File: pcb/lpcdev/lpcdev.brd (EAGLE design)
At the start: 100 x 80 mm, 106 parts, among them IC1 LPC1517BJD48, IC2 DRV8313, IC3 FT231X, IC4 LP2985-3V3, IC5 DRV8313, IC6 DRV8313, Q1 16MHz

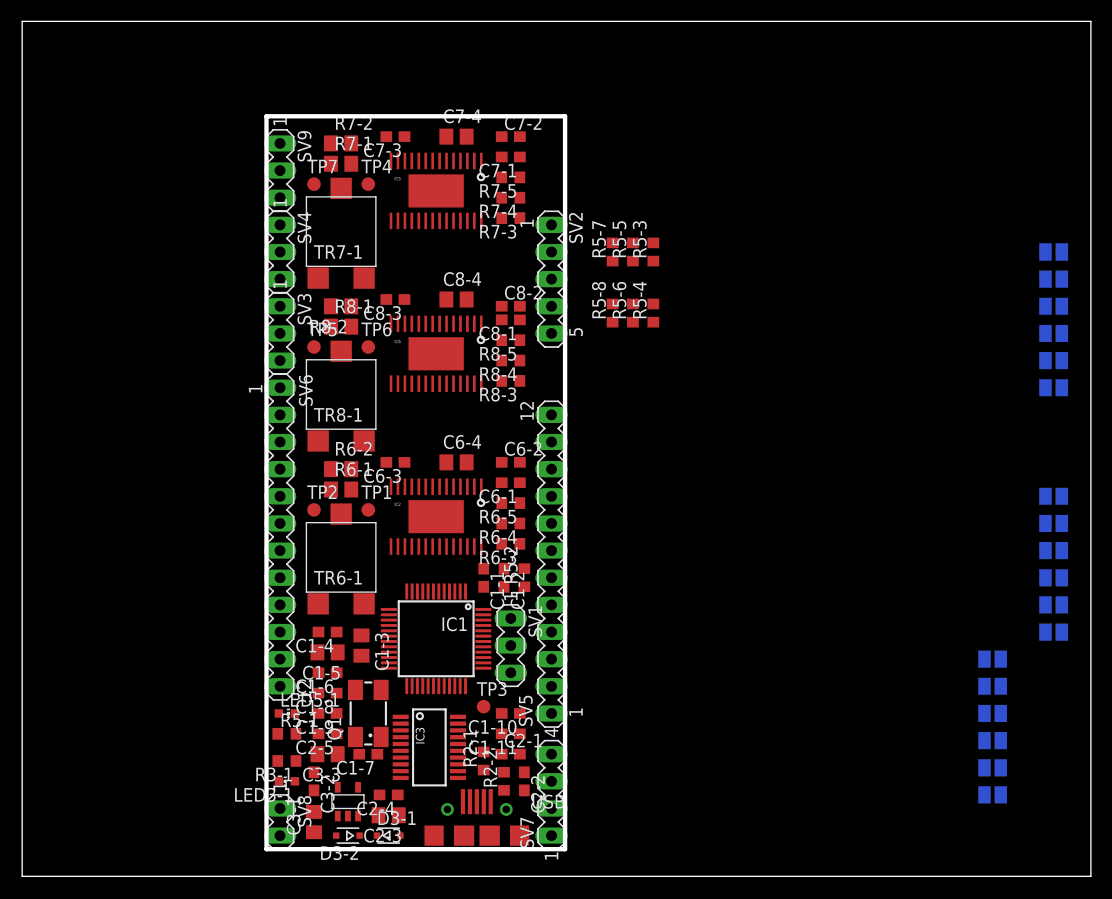
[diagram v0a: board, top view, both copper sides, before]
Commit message: rough routing (no gnd)
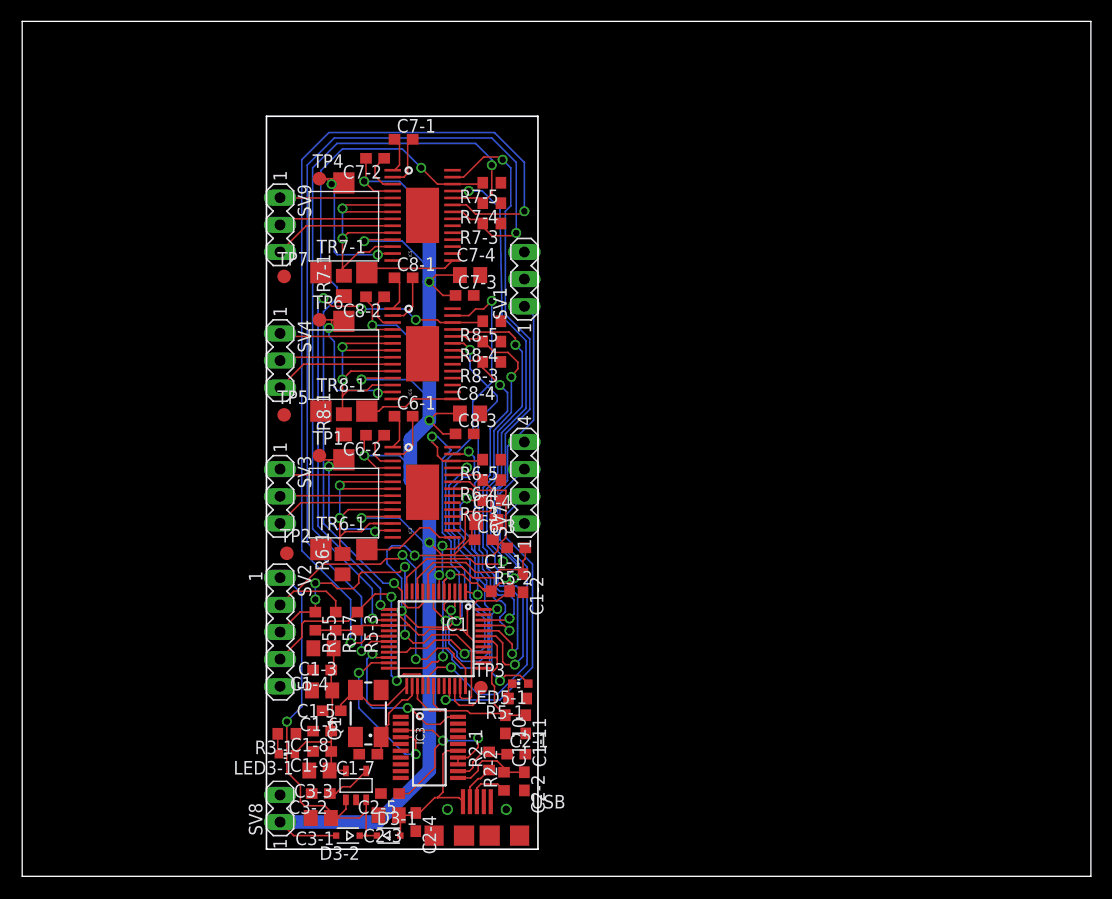
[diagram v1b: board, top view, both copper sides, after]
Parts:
- removed R5-4, R5-6, R5-8: DNM, rcl:R0603
- removed R6-2, R7-2, R8-2: TBD, rcl:R0805
- removed SJ6-1, SJ6-2, SJ6-3, SJ6-4, SJ6-5, SJ6-6, SJ7-1, SJ7-2, SJ7-3, SJ7-4, SJ7-5, SJ7-6, SJ8-1, SJ8-2, SJ8-3, SJ8-4, SJ8-5, SJ8-6: (no value), jumper:SJ
- removed SV5: P1, con-lstb:MA12-1
- removed SV6: P2, con-lstb:MA12-1
- moved R5-5 45.6 mm to (27.4, 23.9), turned to 270 degrees
- moved R5-3 44.3 mm to (31.4, 23.9), turned to 270 degrees
- moved R5-7 43.2 mm to (29.3, 23.9), turned to 270 degrees
- moved SV2 41.7 mm to (24.1, 22.9)
- moved SV1 34.3 mm to (47.0, 55.9), turned to 90 degrees
- moved SV7 29.3 mm to (47.0, 36.8)
- moved LED5-1 22.0 mm to (46.6, 18.0), turned to 90 degrees
- moved R5-1 21.8 mm to (46.4, 16.6), turned to 180 degrees
- moved C7-3 16.2 mm to (41.4, 54.4), turned to 0 degrees
- moved SV3 15.2 mm to (24.1, 35.6)
- moved C8-3 14.1 mm to (41.4, 41.4), turned to 0 degrees
- moved C7-4 13.0 mm to (41.9, 56.3)
- moved C6-2 13.0 mm to (33.0, 41.3), turned to 180 degrees
- moved C7-2 12.9 mm to (33.0, 67.2), turned to 180 degrees
- moved C8-2 12.7 mm to (33.0, 54.2), turned to 180 degrees
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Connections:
- removed net PIO0_0: IC1.1, SJ6-1.2, SV5.2
- removed net PIO0_1: IC1.2, SJ6-2.2, SV5.3
- removed net PIO0_10: IC1.15, SJ7-4.2, SV5.11
- removed net PIO0_11: IC1.18, SJ7-5.2, SV6.1
- removed net PIO0_12: IC1.19, SJ7-6.2, SV6.2
- removed net PIO0_13: IC1.21, SJ8-1.2, SV6.3
- removed net PIO0_18: IC1.13, SJ8-2.2, SV6.4
- removed net PIO0_2: IC1.3, SJ6-3.2, SV5.4
- removed net PIO0_24: IC1.43, SJ8-3.2, SV6.7
- removed net PIO0_25: IC1.44, SJ8-4.2, SV6.8
- removed net PIO0_26: IC1.45, SJ8-5.2, SV6.9
- removed net PIO0_27: IC1.46, SJ8-6.2, SV6.10
- removed net PIO0_3: IC1.4, SJ6-4.2, SV5.5
- removed net PIO0_5: IC1.6, SJ6-5.2, SV5.6
- removed net PIO0_6: IC1.7, SJ6-6.2, SV5.7
- removed net PIO0_7: IC1.8, SJ7-1.2, SV5.8
- removed net PIO0_8: IC1.9, SJ7-2.2, SV5.9
- removed net PIO0_9: IC1.12, SJ7-3.2, SV5.10
- net +3V3: no longer SV5.1
- net DRV1_3V3: now also TR6-1.2; no longer TR6-1.1
- net DRV1_COMPP: no longer R6-2.2
- net DRV1_EN1: now also IC1.2; no longer SJ6-2.1
- net DRV1_EN2: now also IC1.4; no longer SJ6-4.1
- net DRV1_EN3: now also IC1.7; no longer SJ6-6.1
- net DRV1_IN1: now also IC1.1; no longer SJ6-1.1
- net DRV1_IN2: now also IC1.3; no longer SJ6-3.1
- net DRV1_IN3: now also IC1.6; no longer SJ6-5.1
- net DRV2_3V1: now also TR7-1.2; no longer TR7-1.1
- net DRV2_COMPP1: no longer R7-2.2
- net DRV2_EN1: now also IC1.9; no longer SJ7-2.1
- net DRV2_EN2: now also IC1.15; no longer SJ7-4.1
- net DRV2_EN3: now also IC1.19; no longer SJ7-6.1
- net DRV2_IN1: now also IC1.8; no longer SJ7-1.1
- net DRV2_IN2: now also IC1.12; no longer SJ7-3.1
- net DRV2_IN3: now also IC1.18; no longer SJ7-5.1
- net DRV3_3V2: now also TR8-1.2; no longer TR8-1.1
- net DRV3_COMPP2: no longer R8-2.2
- net DRV3_EN1: now also IC1.13; no longer SJ8-2.1
- net DRV3_EN2: now also IC1.44; no longer SJ8-4.1
- net DRV3_EN3: now also IC1.46; no longer SJ8-6.1
- net DRV3_IN1: now also IC1.21; no longer SJ8-1.1
- net DRV3_IN2: now also IC1.43; no longer SJ8-3.1
- net DRV3_IN3: now also IC1.45; no longer SJ8-5.1
- net GND: now also TR6-1.1, TR7-1.1, TR8-1.1; no longer R5-4.1, R5-6.1, R5-8.1, R6-2.1, R7-2.1, R8-2.1, SV5.12, TR6-1.2, TR7-1.2, TR8-1.2
- net PIO0_22: no longer SV6.5
- net PIO0_23: no longer SV6.6
- net PIO0_28: no longer SV6.11
- net PIO0_29: no longer SV6.12
- net QEI_IDX: no longer R5-4.2
- net QEI_PHA: no longer R5-8.2
- net QEI_PHB: no longer R5-6.2
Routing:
- net +12V: track 0.00 -> 159.2 mm, vias 0 -> 9
- net +3V3: track 0.00 -> 87.1 mm
- net DRV2_EN3: track 0.00 -> 85.8 mm, vias 0 -> 2
- net DRV2_IN3: track 0.00 -> 85.7 mm, vias 0 -> 2
- net DRV2_EN2: track 0.00 -> 71.9 mm, vias 0 -> 2
- net DRV2_EN1: track 0.00 -> 66.0 mm, vias 0 -> 2
- net DRV2_IN1: track 0.00 -> 58.4 mm, vias 0 -> 2
- net DRV2_IN2: track 0.00 -> 52.3 mm, vias 0 -> 2
- net ISP_01: track 0.00 -> 51.1 mm, vias 0 -> 3
- net DRV3_IN1: track 0.00 -> 50.3 mm, vias 0 -> 2
- net DRV3_EN1: track 0.00 -> 48.2 mm, vias 0 -> 4
- net DRV3_IN2: track 0.00 -> 46.0 mm, vias 0 -> 2
- net DRV3_EN2: track 0.00 -> 42.1 mm, vias 0 -> 2
- net DRV1_EN2: track 0.00 -> 37.9 mm, vias 0 -> 2
- net REG_VIN: track 0.00 -> 37.9 mm, vias 0 -> 1
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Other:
- outline, holes or cut-outs redrawn

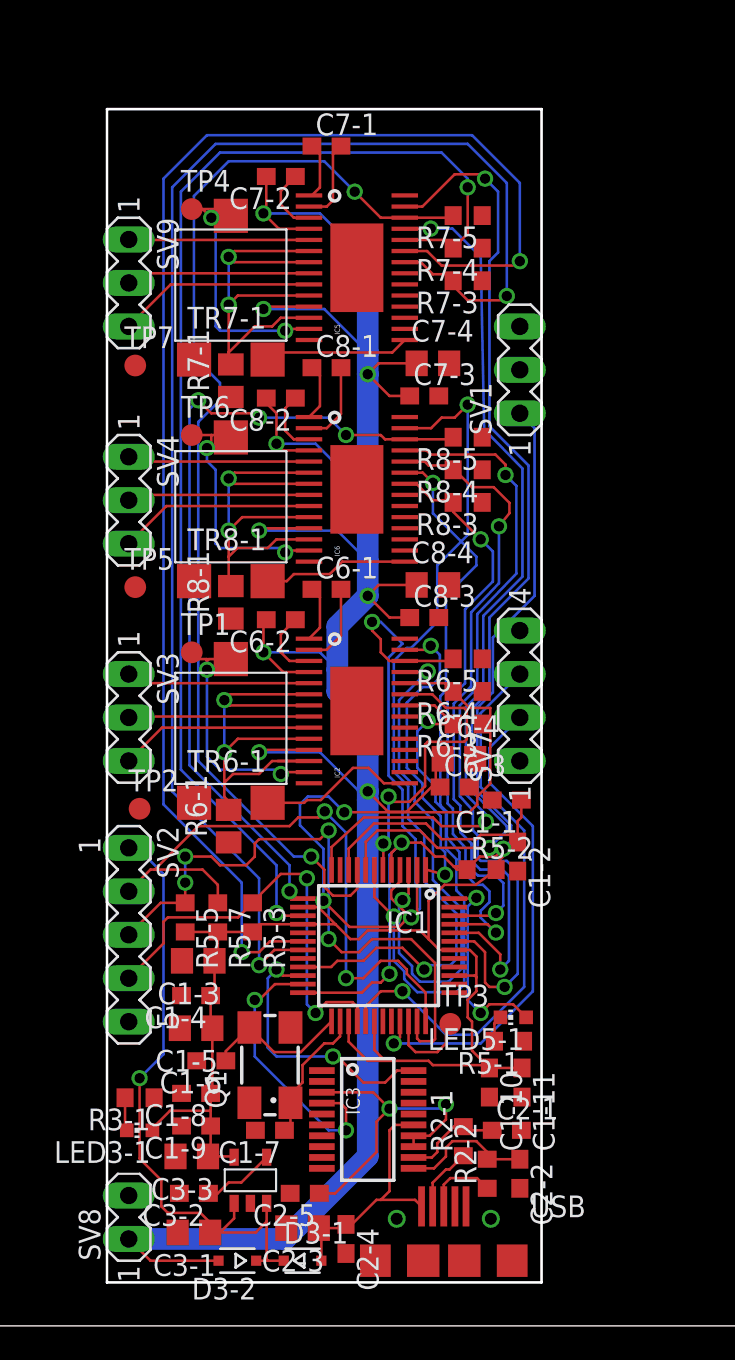
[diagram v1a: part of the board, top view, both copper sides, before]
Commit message: Routing complete, ERC and DRC is OK
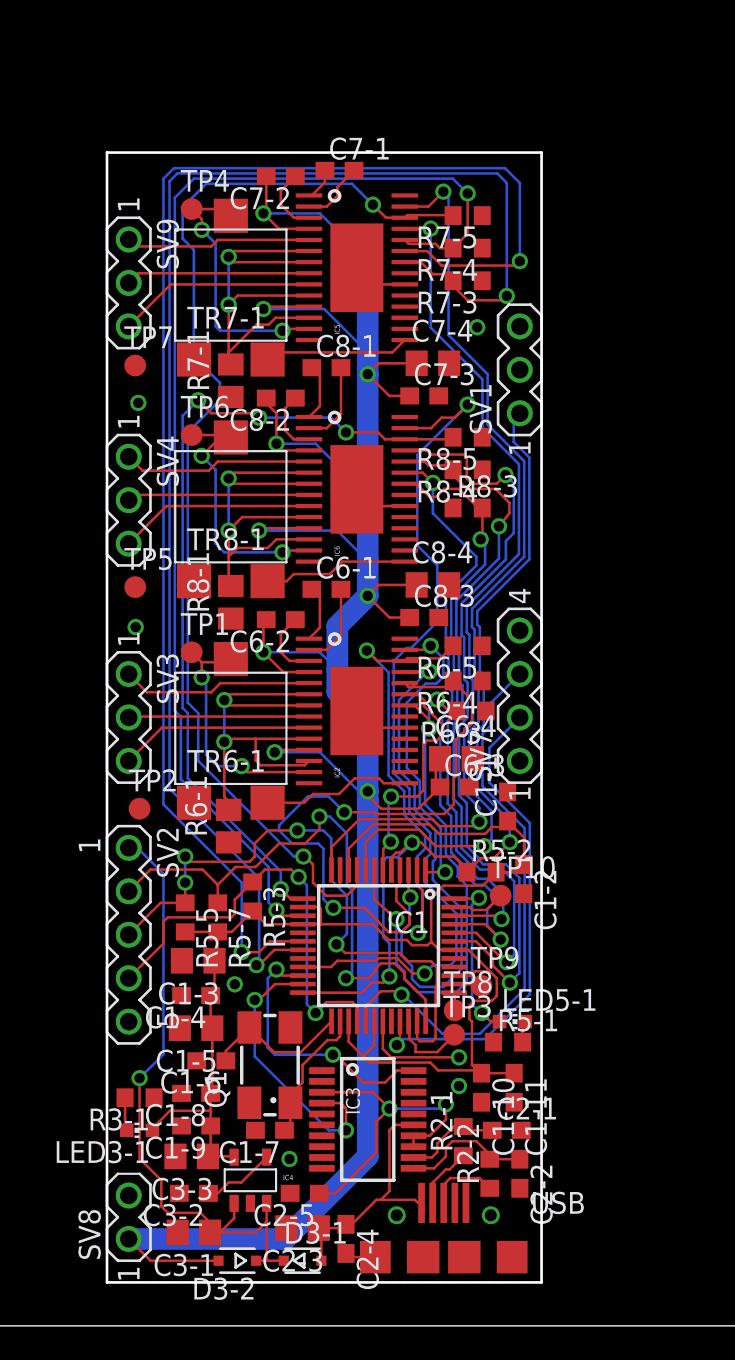
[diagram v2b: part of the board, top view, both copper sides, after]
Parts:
- added TP10, TP8, TP9: TPB1,27, testpad:B1,27
- SV1, SV3, SV4, SV9: device con-lstb:MA03-1 -> lpclib:MA03-1
- SV2: device con-lstb:MA05-1 -> lpclib:MA05-1
- SV7: device con-lstb:MA04-1 -> lpclib:MA04-1
- moved C7-1 1.61 mm to (36.4, 67.5)
- moved C1-2 1.37 mm to (47.2, 26.1)
- moved R5-3 1.22 mm to (31.4, 25.1)
- moved R6-3 0.80 mm to (44.2, 35.9)
- moved R6-5 0.76 mm to (43.9, 39.8)
- moved TP3 0.67 mm to (43.2, 17.0)
- moved R6-4 0.61 mm to (43.9, 37.7)
- moved C1-10 0.55 mm to (44.8, 13.9)
- moved C1-11 0.55 mm to (46.7, 13.9)
- moved C1-1 0.38 mm to (46.3, 30.4), turned to 90 degrees
- moved R8-3 0.33 mm to (43.9, 47.8), turned to 0 degrees
- moved LED5-1 0.26 mm to (46.6, 17.8), turned to 270 degrees
- moved USB 0.20 mm to (42.5, 4.01)
- moved C6-4 0.15 mm to (43.3, 33.1)
- moved R2-2 0.15 mm to (45.2, 8.89)
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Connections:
- net PIO0_22: now also TP8.TP
- net PIO0_23: now also TP9.TP
- net PIO0_28: now also TP10.TP
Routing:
- net GND: track 0.00 -> 18.5 mm, vias 0 -> 7
- net DRV2_IN1: track 58.4 -> 54.4 mm
- net DRV1_IN3: track 17.8 -> 14.5 mm
- net PIO0_28: track 0.00 -> 3.13 mm
- net DRV1_COMPP: track 29.3 -> 26.3 mm
- net QEI_PHA: track 36.4 -> 33.6 mm
- net +3V3: track 87.1 -> 89.2 mm
- net DRV3_EN3: track 34.0 -> 36.0 mm
- net PIO0_29: track 11.7 -> 9.89 mm
- net +12V: track 159.2 -> 157.4 mm
- net DRV1_EN2: track 37.9 -> 39.6 mm
- net ISP_01: track 51.1 -> 52.8 mm
- net PIO0_23: track 0.00 -> 1.64 mm
- net DRV2_IN3: track 85.7 -> 84.1 mm
- net DRV2_EN2: track 71.9 -> 70.3 mm
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- added copper zone on layer 1, net GND
- added copper zone on layer 16, net GND
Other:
- outline, holes or cut-outs redrawn

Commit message: final touchup and gerber generating
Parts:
- removed LED5-1: Green, led:CHIP-LED0603
- removed SV1: ISP, lpclib:MA03-1
- removed SV2: ENCODER, lpclib:MA05-1
- removed SV3, SV4, SV9: MOTOR, lpclib:MA03-1
- removed SV7: SWD, lpclib:MA04-1
- removed SV8: +12V, lpclib:MA02-1
- removed TP1, TP10, TP3, TP4, TP6, TP8, TP9: TPB1,27, testpad:B1,27
- added !R, ILIM1, ILIM2, ILIM3: TPB1,27, testpad:B1,27
- added +12V: +12V, lpclib:MA02-1
- added ENC: ENCODER, lpclib:MA05-1
- added GPIO: GPIO, lpclib:MA03-1
- added ISP: ISP, lpclib:MA03-1
- added L029: Green, led:CHIP-LED0603
- added M1, M2, M3: MOTOR, lpclib:MA03-1
- added SWD: SWD, lpclib:MA04-1
- moved R5-1 24.1 mm to (22.4, 13.7), turned to 90 degrees
- moved C1-10 23.9 mm to (21.0, 11.3)
- moved C1-11 23.6 mm to (23.3, 10.6), turned to 0 degrees
- moved C1-1 23.5 mm to (23.0, 27.8)
- moved C8-1 23.3 mm to (12.6, 52.9)
- moved R7-1 23.1 mm to (7.24, 52.2)
- moved C8-2 23.0 mm to (10.2, 51.5)
- moved C2-1 23.0 mm to (23.4, 8.84)
- moved C2-2 23.0 mm to (24.1, 6.30)
- moved C6-2 23.0 mm to (10.2, 38.7)
- moved C7-2 23.0 mm to (10.2, 64.6)
- moved IC2 23.0 mm to (14.6, 33.4)
- moved IC5 23.0 mm to (14.6, 59.3)
- moved IC6 23.0 mm to (14.6, 46.3)
- moved R2-1 23.0 mm to (20.8, 8.20)
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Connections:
- net !RESET: now also !R.TP; no longer TP3.TP
- net +12V: now also +12V.1; no longer SV8.1
- net DRV1_COMPN: now also ILIM1.TP; no longer TP1.TP
- net DRV1_OUT1: now also M1.1; no longer SV3.1
- net DRV1_OUT2: now also M1.2; no longer SV3.2
- net DRV1_OUT3: now also M1.3; no longer SV3.3
- net DRV2_COMPN1: now also ILIM2.TP; no longer TP4.TP
- net DRV2_OUT1: now also M2.1; no longer SV9.1
- net DRV2_OUT2: now also M2.2; no longer SV9.2
- net DRV2_OUT3: now also M2.3; no longer SV9.3
- net DRV3_COMPN2: now also ILIM3.TP; no longer TP6.TP
- net DRV3_OUT1: now also M3.1; no longer SV4.1
- net DRV3_OUT2: now also M3.2; no longer SV4.2
- net DRV3_OUT3: now also M3.3; no longer SV4.3
- net GND: now also +12V.2, ENC.5, ISP.2, SWD.4; no longer SV1.2, SV2.5, SV7.4, SV8.2
- net ISP_01: now also ISP.1; no longer SV1.1
- net LED1: now also L029.C; no longer LED5-1.C
- net PIO0_22: now also GPIO.1; no longer TP8.TP
- net PIO0_23: now also GPIO.2; no longer TP9.TP
- net PIO0_28: now also GPIO.3; no longer TP10.TP
- net PIO0_29: now also L029.A; no longer LED5-1.A
- net QEI_IDX: now also ENC.4; no longer SV2.4
- net QEI_PHA: now also ENC.2; no longer SV2.2
- net QEI_PHB: now also ENC.3; no longer SV2.3
- net REG_VIN: now also ENC.1; no longer SV2.1
- net SWCLK: now also SWD.3; no longer SV7.3
- net SWDIO: now also SWD.2; no longer SV7.2
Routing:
- net +12V: track 157.4 -> 145.9 mm
- net PIO0_22: track 1.07 -> 7.10 mm
- net PIO0_28: track 3.13 -> 7.71 mm
- net DRV3_EN1: track 49.1 -> 53.0 mm, vias 4 -> 2
- net GND: track 18.5 -> 15.1 mm, vias 7 -> 35
- net PIO0_23: track 1.64 -> 4.92 mm
- net DRV3_IN2: track 46.1 -> 42.8 mm
- net DRV3_IN3: track 35.9 -> 33.5 mm
- net DRV3_EN2: track 42.0 -> 39.6 mm
- net PIO0_29: track 9.89 -> 10.8 mm
- net !RESET: track 4.66 -> 3.97 mm
- net DRV2_EN1: track 66.1 -> 66.7 mm
- net DRV3_CPH2: track 4.92 -> 4.36 mm
- net DRV3_EN3: track 36.0 -> 35.5 mm
- net +3V3: track 89.2 -> 89.3 mm, vias 0 -> 2
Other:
- board size 100 x 80 mm -> 25.4 x 66 mm
- board text added: "028 023 022"
- board text added: "Gimbal controller - rev1"
- board text added: "dlofstrom"
